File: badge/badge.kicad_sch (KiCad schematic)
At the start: 21 parts, among them SW1 SW_Push

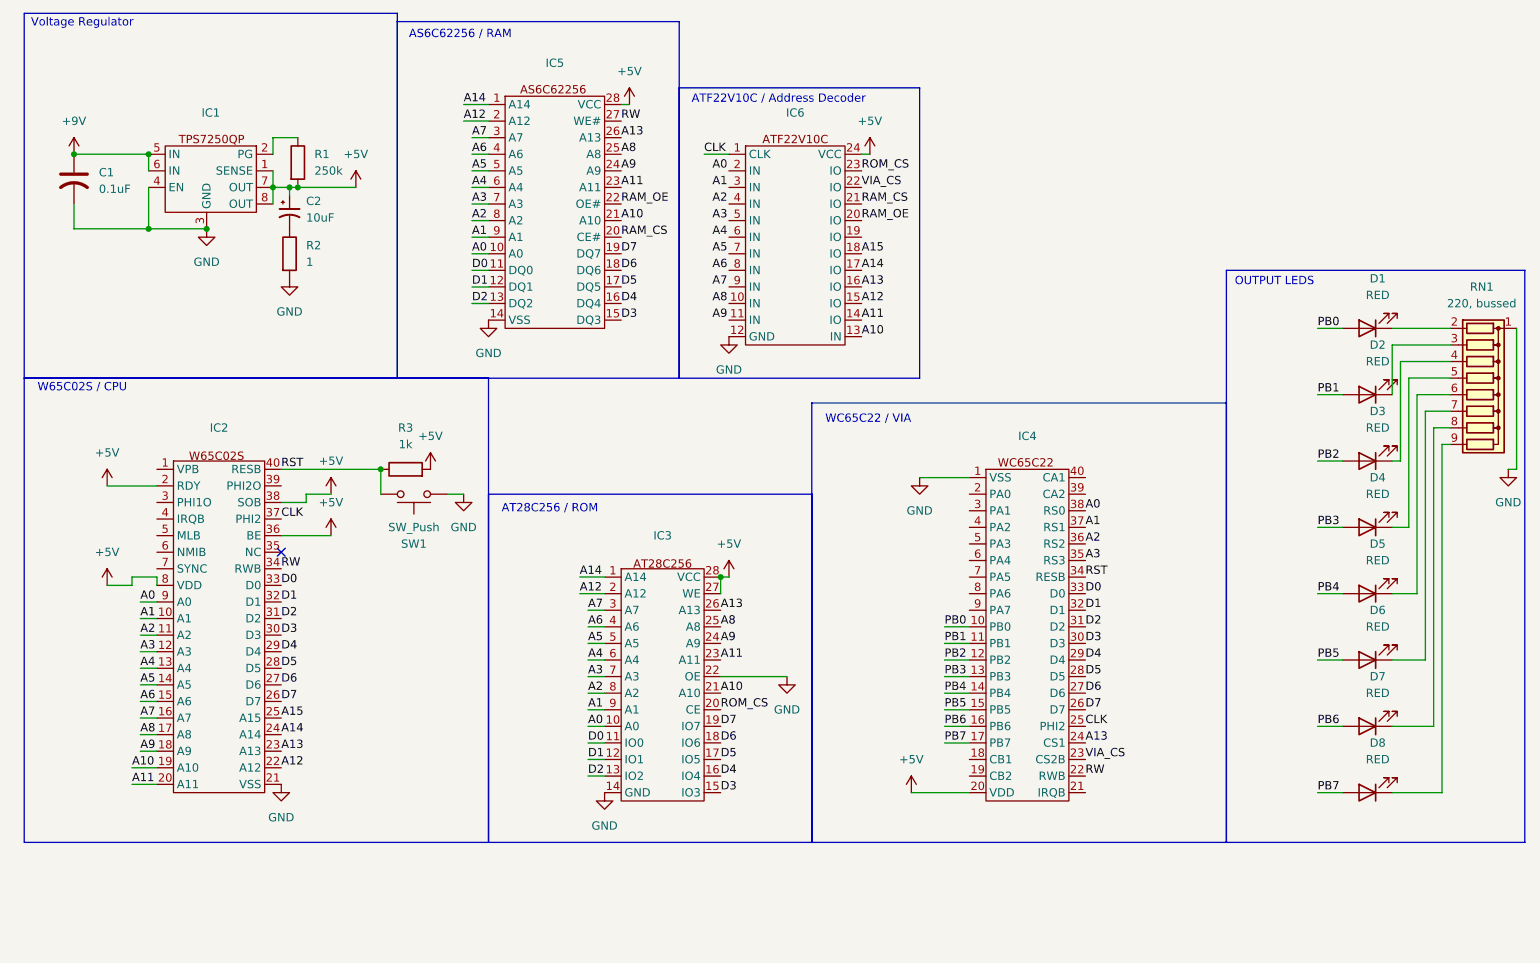
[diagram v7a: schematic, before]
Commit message: Add UART serial
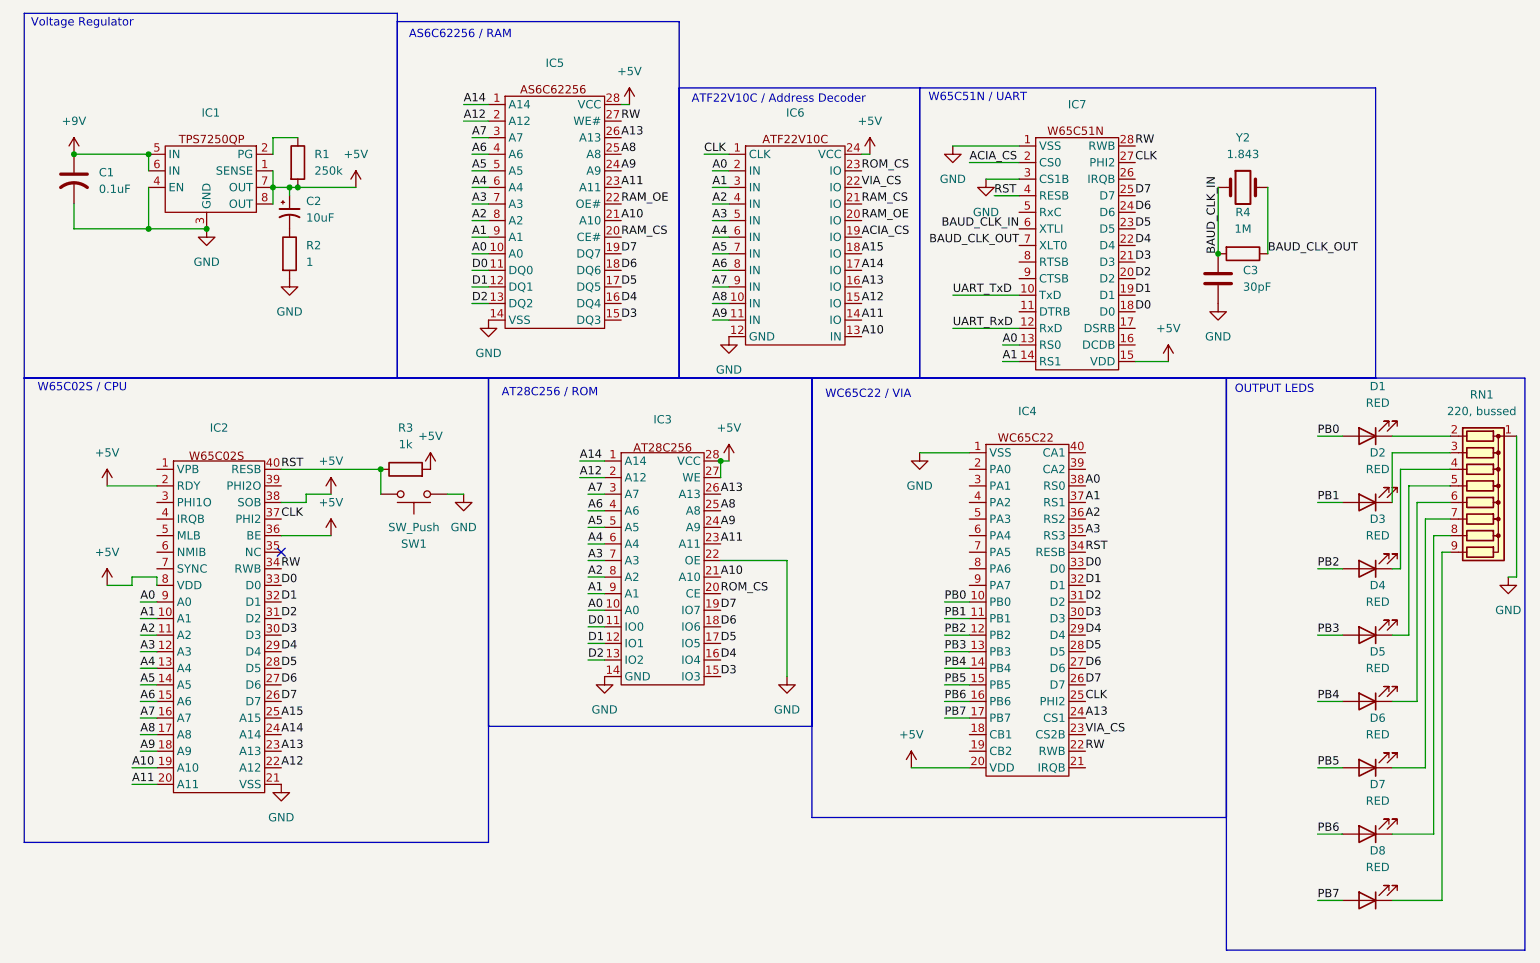
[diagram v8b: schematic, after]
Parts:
- added C3: 30pF, symbol Device:C
- added IC7: ~, symbol 6502ConferenceBadge:W65C51N
- added R4: 1M, symbol Device:R
- added Y2: 1.843, symbol Device:Crystal
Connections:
- net +5V: now also IC7.15 (VDD)
- net A0: now also IC6.2 (IN), IC7.13 (RS0)
- net A1: now also IC6.3 (IN), IC7.14 (RS1)
- net A2: now also IC6.4 (IN)
- net A3: now also IC6.5 (IN)
- net A4: now also IC6.6 (IN)
- net A5: now also IC6.7 (IN)
- net A6: now also IC6.8 (IN)
- net A7: now also IC6.9 (IN)
- net A8: now also IC6.10 (IN)
- net A9: now also IC6.11 (IN)
- net CLK: now also IC7.27 (PHI2)
- net D0: now also IC7.18 (D0)
- net D1: now also IC7.19 (D1)
- net D2: now also IC7.20 (D2)
- net D3: now also IC7.21 (D3)
- net D4: now also IC7.22 (D4)
- net D5: now also IC7.23 (D5)
- net D6: now also IC7.24 (D6)
- net D7: now also IC7.25 (D7)
- net GND: now also C3.2, IC7.1 (VSS), IC7.3 (CS1B)
- net RST: now also IC7.4 (RESB)
- net RW: now also IC7.28 (RWB)
- net ACIA_CS: now reaches IC6.19 (IO)
- net ACIA_CS: now also IC7.2 (CS0)
- new net BAUD_CLK_IN: C3.1, IC7.6 (XTLI), R4.2, Y2.1
- new net BAUD_CLK_OUT: IC7.7 (XLT0), R4.1, Y2.2
- new net UART_RxD: IC7.12 (RxD)
- new net UART_TxD: IC7.10 (TxD)
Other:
- note added: "W65C51N / UART"
- moved on the sheet: D1, D2, D3, D4, D5, D6, D7, D8, IC3, IC4, RN1
